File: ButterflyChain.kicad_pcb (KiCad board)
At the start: 2 copper layers, 93.1 x 65.5 mm, 30 parts, among them J2 USB_A, J3 Conn_01x02, SW1 SW_Push, U1 ATTINY85-20PU

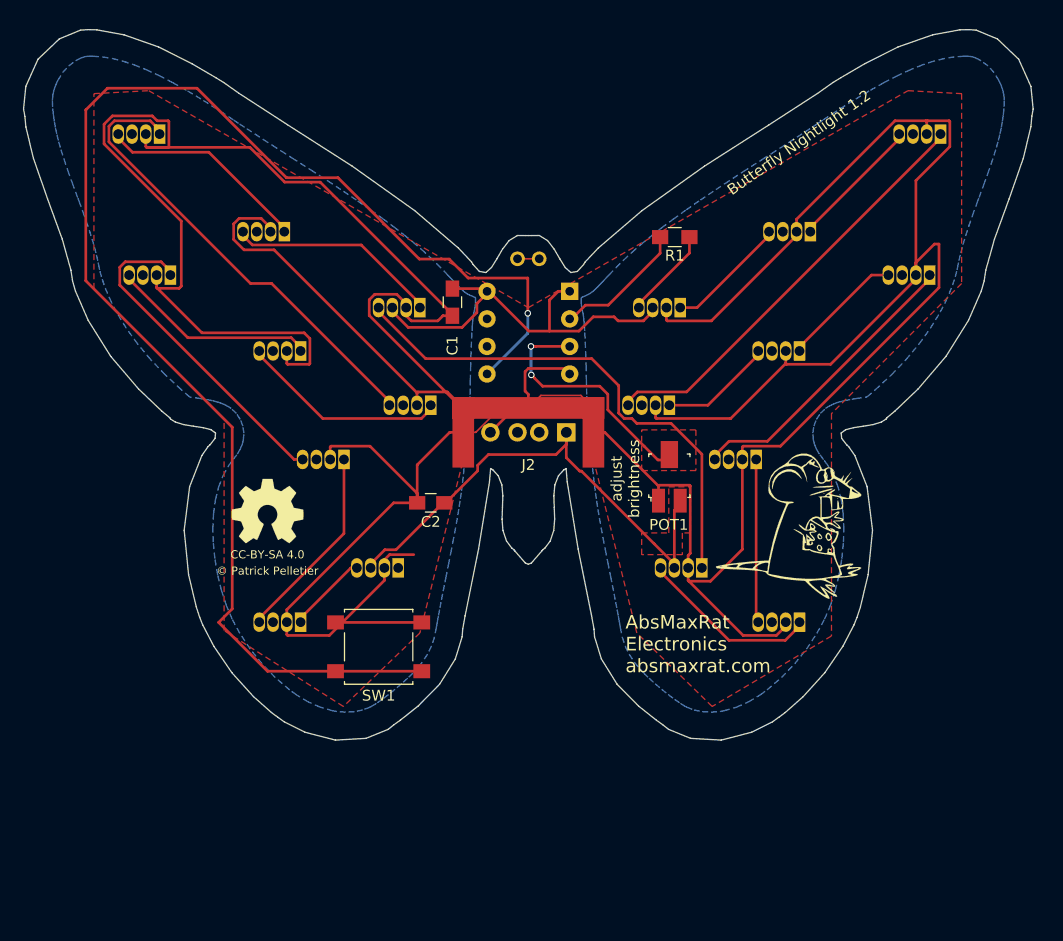
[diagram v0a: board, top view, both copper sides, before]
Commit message: Remove old footprints.
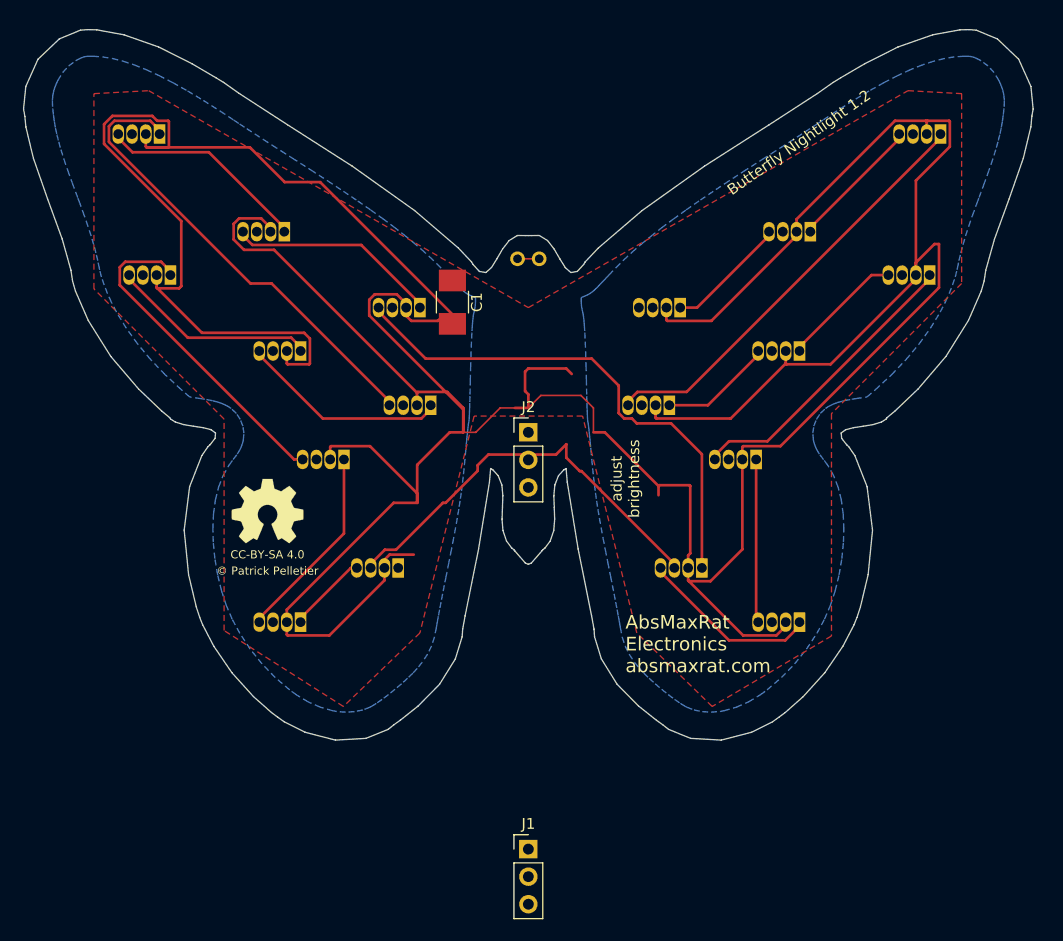
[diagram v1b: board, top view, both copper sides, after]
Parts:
- removed C2: 10uF, Capacitors_SMD:C_0805_HandSoldering
- removed the G*** at (124.2, 118.8)
- removed POT1: TC33X-2-103E, digikey-footprints:TC33X-2-103E
- removed R1: 470, Resistors_SMD:R_0805_HandSoldering
- removed SW1: SW_Push, Buttons_Switches_SMD:SW_SPST_B3S-1000
- removed U1: ATTINY85-20PU, myLibrary:DIP-8_W7.62mm
- added J1: Input, Pin_Headers:Pin_Header_Straight_1x03_Pitch2.54mm, F.Cu at (100.1, 148.7)
- C1: value 0.1uF -> 47µF; footprint Capacitors_SMD:C_0805_HandSoldering -> Capacitors_SMD:C_1210_HandSoldering
- J2: value USB_A -> Output; footprint myLibrary:USB_A_Molex-0480370001_Vertical -> Pin_Headers:Pin_Header_Straight_1x03_Pitch2.54mm
- J3: value Conn_01x02 -> Antennae
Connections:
- J2 pad 2: Net-(J2-Pad2) -> Net-(D18-Pad1)
- J2 pad 3: Net-(J2-Pad3) -> GND
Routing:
- net Net-(SW1-Pad2): track 133.2 -> 0.00 mm, vias 1 -> 0
- net +5V: track 86.3 -> 39.6 mm
- net Net-(POT1-Pad2): track 23.2 -> 0.00 mm, vias 2 -> 0
- net Net-(R1-Pad2): track 12.1 -> 0.00 mm
- net GND: track 409.6 -> 398.5 mm
- net Net-(D1-Pad4): track 8.43 -> 0.36 mm
- removed copper zone on F.Cu, net +5V
- removed copper zone on F.Cu, net Net-(POT1-Pad2)

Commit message: Change filled zones.
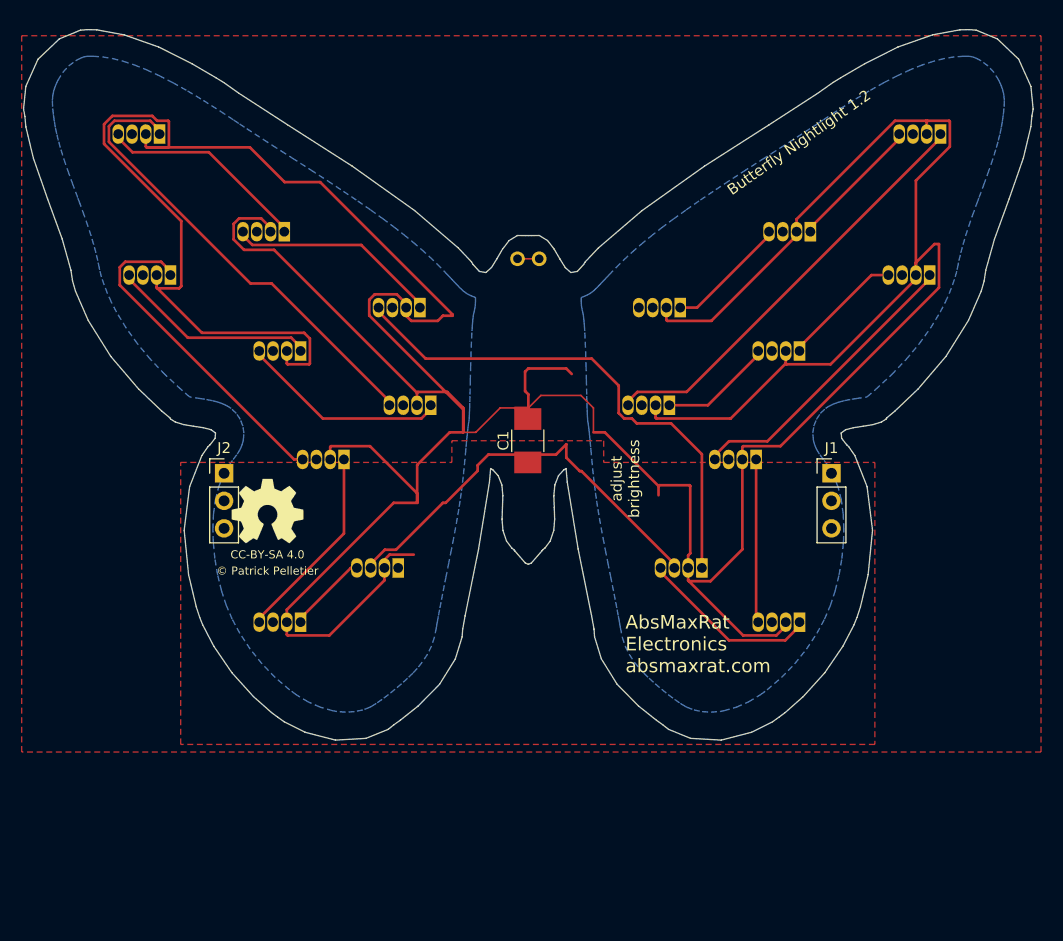
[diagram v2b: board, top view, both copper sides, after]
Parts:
- moved J1 44.5 mm to (128.0, 114.0)
- moved J2 28.3 mm to (72.0, 114.0)
- moved C1 14.5 mm to (100.0, 111.0), turned to 90 degrees
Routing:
- added copper zone on F.Cu, net +5V
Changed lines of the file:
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@@
   )
   (module Capacitors_SMD:C_1210_HandSoldering (layer F.Cu)
-    (at 93.053006 98.22564 270)
+    (at 100 111 90)
     (descr "Capacitor SMD 1210, hand soldering")
     (tags "capacitor 1210")
     (attr smd)
-    (fp_text reference C1 (at 0 -2.25 270) (layer F.SilkS)
-      (effects (font (size 1 1) (thickness 0.15)))
-    )
-    (fp_text value 47µF (at 0 2.5 270) (layer F.Fab)
-      (effects (font (size 1 1) (thickness 0.15)))
-    )
-    (fp_text user %R (at 0 -2.25 270) (layer F.Fab)
+    (fp_text reference C1 (at 0 -2.25 90) (layer F.SilkS)
+      (effects (font (size 1 1) (thickness 0.15)))
+    )
+    (fp_text value 47µF (at 0 2.5 90) (layer F.Fab)
+      (effects (font (size 1 1) (thickness 0.15)))
+    )
+    (fp_text user %R (at 0 -2.25 90) (layer F.Fab)
       (effects (font (size 1 1) (thickness 0.15)))
     )
@@
     (fp_line (start 3.25 1.5) (end 3.25 -1.5) (layer F.CrtYd) (width 0.05))
     (fp_line (start 3.25 1.5) (end -3.25 1.5) (layer F.CrtYd) (width 0.05))
-    (pad 1 smd rect (at -2 0 270) (size 2 2.5) (layers F.Cu F.Paste F.Mask)
+    (pad 1 smd rect (at -2 0 90) (size 2 2.5) (layers F.Cu F.Paste F.Mask)
       (net 1 +5V))
-    (pad 2 smd rect (at 2 0 270) (size 2 2.5) (layers F.Cu F.Paste F.Mask)
+    (pad 2 smd rect (at 2 0 90) (size 2 2.5) (layers F.Cu F.Paste F.Mask)
       (net 2 GND))
     (model Capacitors_SMD.3dshapes/C_1210.wrl
@@
   )
   (module Pin_Headers:Pin_Header_Straight_1x03_Pitch2.54mm (layer F.Cu)
-    (at 100.053006 148.651281)
+    (at 128 114)
     (descr "Through hole straight pin header, 1x03, 2.54mm pitch, single row")
     (tags "Through hole pin header THT 1x03 2.54mm single row")
@@
   )
   (module Pin_Headers:Pin_Header_Straight_1x03_Pitch2.54mm (layer F.Cu)
-    (at 100.053006 110.22564)
+    (at 72 114)
     (descr "Through hole straight pin header, 1x03, 2.54mm pitch, single row")
     (tags "Through hole pin header THT 1x03 2.54mm single row")
@@
     (connect_pads (clearance 0.3048))
     (min_thickness 0.254)
-    (fill yes (arc_segments 16) (thermal_gap 0.508) (thermal_bridge_width 0.508))
+    (fill (arc_segments 16) (thermal_gap 0.508) (thermal_bridge_width 0.508))
     (polygon
       (pts
-        (xy 100.053006 98.72564) (xy 135.053006 78.72564) (xy 140 79) (xy 140 96.5) (xy 128 108.5)
-        (xy 128 129) (xy 117 135.5) (xy 110.053006 128.72564) (xy 105.053006 108.72564) (xy 95.053006 108.72564)
-        (xy 90.053006 128.72564) (xy 83 135.5) (xy 72 128.5) (xy 72 109) (xy 60 97)
-        (xy 60 79) (xy 65.053006 78.72564)
+        (xy 147.32 139.7) (xy 53.34 139.7) (xy 53.34 73.66) (xy 147.32 73.66)
       )
     )
+  )
+  (zone (net 1) (net_name +5V) (layer F.Cu) (hatch edge 0.508)
+    (priority 1)
+    (connect_pads (clearance 0.3048))
+    (min_thickness 0.254)
+    (fill (arc_segments 16) (thermal_gap 0.508) (thermal_bridge_width 0.508))
+    (polygon
+      (pts
+        (xy 107 113) (xy 132 113) (xy 132 139) (xy 68 139) (xy 68 113)
+        (xy 93 113) (xy 93 111) (xy 107 111)
+      )
+    )

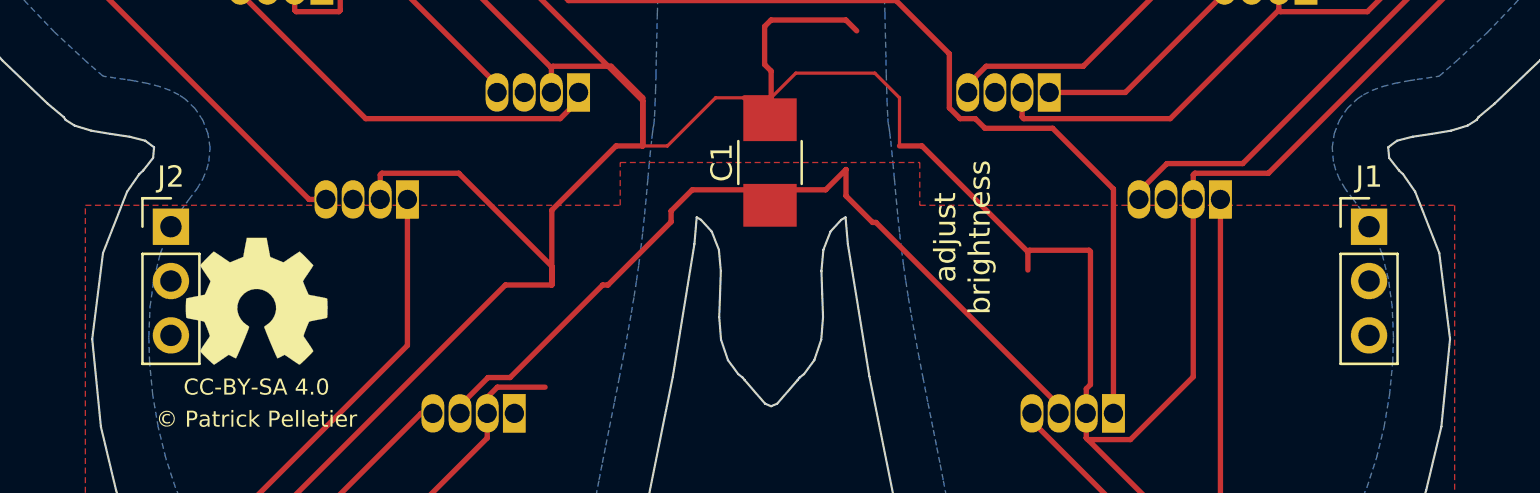
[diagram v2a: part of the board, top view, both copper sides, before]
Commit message: Adjust angle of J1 and J2.
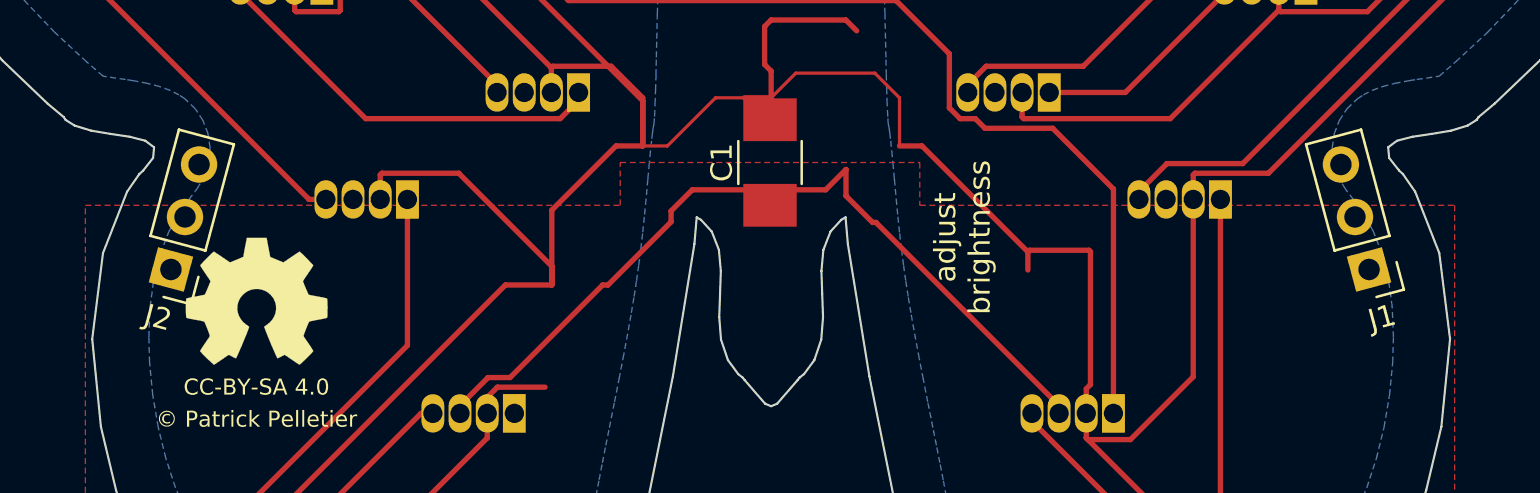
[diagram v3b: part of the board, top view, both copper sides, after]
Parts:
- moved J1 2.00 mm to (128.0, 116.0), turned to 195 degrees
- moved J2 2.00 mm to (72.0, 116.0), turned to 165 degrees
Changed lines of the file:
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@@
   )
   (module Pin_Headers:Pin_Header_Straight_1x03_Pitch2.54mm (layer F.Cu)
-    (at 128 114)
+    (at 128 116 195)
     (descr "Through hole straight pin header, 1x03, 2.54mm pitch, single row")
     (tags "Through hole pin header THT 1x03 2.54mm single row")
-    (fp_text reference J1 (at 0 -2.33) (layer F.SilkS)
+    (fp_text reference J1 (at 0 -2.33 195) (layer F.SilkS)
       (effects (font (size 1 1) (thickness 0.15)))
     )
-    (fp_text value Input (at 0 7.41) (layer F.Fab)
+    (fp_text value Input (at 0 7.41 195) (layer F.Fab)
       (effects (font (size 1 1) (thickness 0.15)))
     )
@@
     (fp_line (start 1.8 6.85) (end 1.8 -1.8) (layer F.CrtYd) (width 0.05))
     (fp_line (start 1.8 -1.8) (end -1.8 -1.8) (layer F.CrtYd) (width 0.05))
-    (fp_text user %R (at 0 2.54 90) (layer F.Fab)
+    (fp_text user %R (at 0 2.54 285) (layer F.Fab)
       (effects (font (size 1 1) (thickness 0.15)))
     )
-    (pad 1 thru_hole rect (at 0 0) (size 1.7 1.7) (drill 1) (layers *.Cu *.Mask)
+    (pad 1 thru_hole rect (at 0 0 195) (size 1.7 1.7) (drill 1) (layers *.Cu *.Mask)
       (net 1 +5V))
-    (pad 2 thru_hole oval (at 0 2.54) (size 1.7 1.7) (drill 1) (layers *.Cu *.Mask)
+    (pad 2 thru_hole oval (at 0 2.54 195) (size 1.7 1.7) (drill 1) (layers *.Cu *.Mask)
       (net 4 "Net-(D1-Pad4)"))
-    (pad 3 thru_hole oval (at 0 5.08) (size 1.7 1.7) (drill 1) (layers *.Cu *.Mask)
+    (pad 3 thru_hole oval (at 0 5.08 195) (size 1.7 1.7) (drill 1) (layers *.Cu *.Mask)
       (net 2 GND))
     (model ${KISYS3DMOD}/Pin_Headers.3dshapes/Pin_Header_Straight_1x03_Pitch2.54mm.wrl
@@
   )
   (module Pin_Headers:Pin_Header_Straight_1x03_Pitch2.54mm (layer F.Cu)
-    (at 72 114)
+    (at 72 116 165)
     (descr "Through hole straight pin header, 1x03, 2.54mm pitch, single row")
     (tags "Through hole pin header THT 1x03 2.54mm single row")
-    (fp_text reference J2 (at 0 -2.33) (layer F.SilkS)
+    (fp_text reference J2 (at 0 -2.33 165) (layer F.SilkS)
       (effects (font (size 1 1) (thickness 0.15)))
     )
-    (fp_text value Output (at 0 7.41) (layer F.Fab)
+    (fp_text value Output (at 0 7.41 165) (layer F.Fab)
       (effects (font (size 1 1) (thickness 0.15)))
     )
@@
     (fp_line (start 1.8 6.85) (end 1.8 -1.8) (layer F.CrtYd) (width 0.05))
     (fp_line (start 1.8 -1.8) (end -1.8 -1.8) (layer F.CrtYd) (width 0.05))
-    (fp_text user %R (at 0 2.54 90) (layer F.Fab)
+    (fp_text user %R (at 0 2.54 255) (layer F.Fab)
       (effects (font (size 1 1) (thickness 0.15)))
     )
-    (pad 1 thru_hole rect (at 0 0) (size 1.7 1.7) (drill 1) (layers *.Cu *.Mask)
+    (pad 1 thru_hole rect (at 0 0 165) (size 1.7 1.7) (drill 1) (layers *.Cu *.Mask)
       (net 1 +5V))
-    (pad 2 thru_hole oval (at 0 2.54) (size 1.7 1.7) (drill 1) (layers *.Cu *.Mask)
+    (pad 2 thru_hole oval (at 0 2.54 165) (size 1.7 1.7) (drill 1) (layers *.Cu *.Mask)
       (net 21 "Net-(D18-Pad1)"))
-    (pad 3 thru_hole oval (at 0 5.08) (size 1.7 1.7) (drill 1) (layers *.Cu *.Mask)
+    (pad 3 thru_hole oval (at 0 5.08 165) (size 1.7 1.7) (drill 1) (layers *.Cu *.Mask)
       (net 2 GND))
     (model ${KISYS3DMOD}/Pin_Headers.3dshapes/Pin_Header_Straight_1x03_Pitch2.54mm.wrl
